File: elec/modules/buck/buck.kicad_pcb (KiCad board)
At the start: 2 copper layers, 35.6 x 40.6 mm, 18 parts, among them J1 Conn_01x08, J2 Conn_01x08, U2 TPS5430DDAG4, U3 TPS5430DDAG4

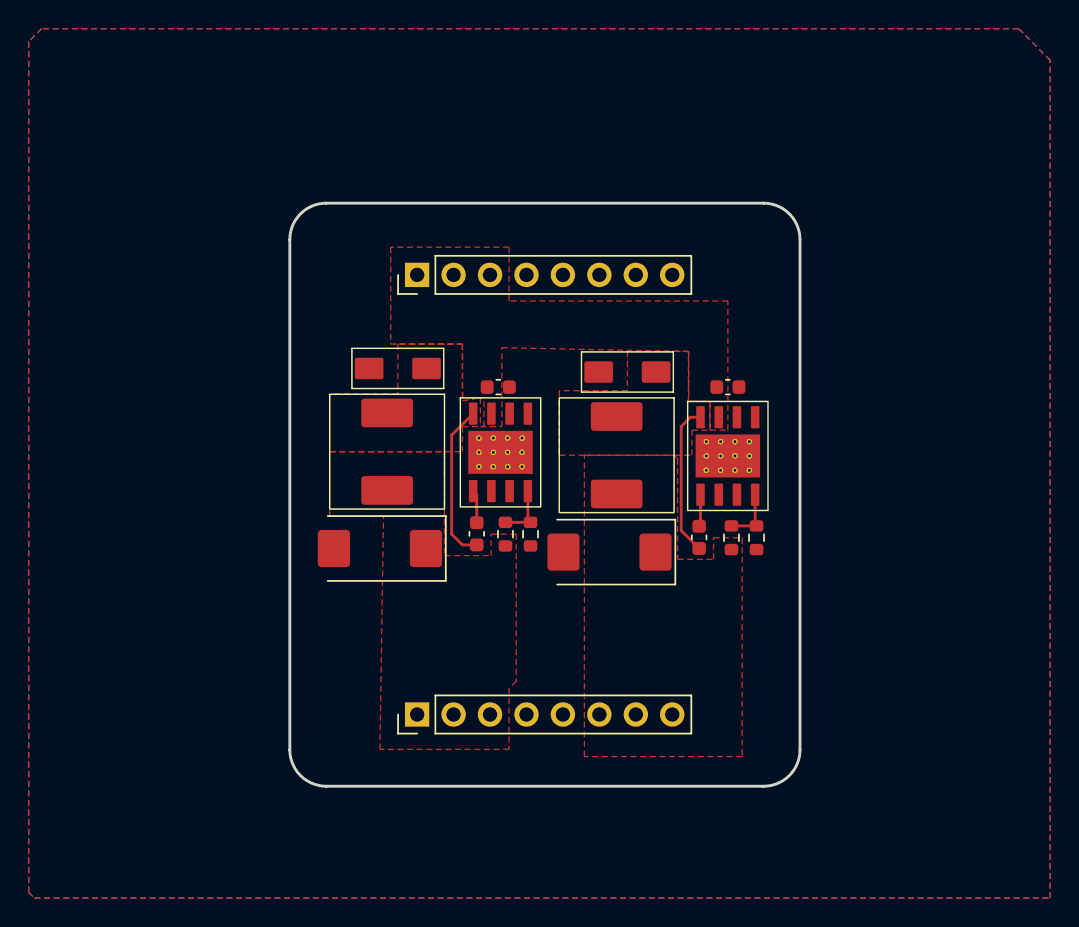
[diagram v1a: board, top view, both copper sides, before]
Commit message: Finished slaving avay buck done +PCBA
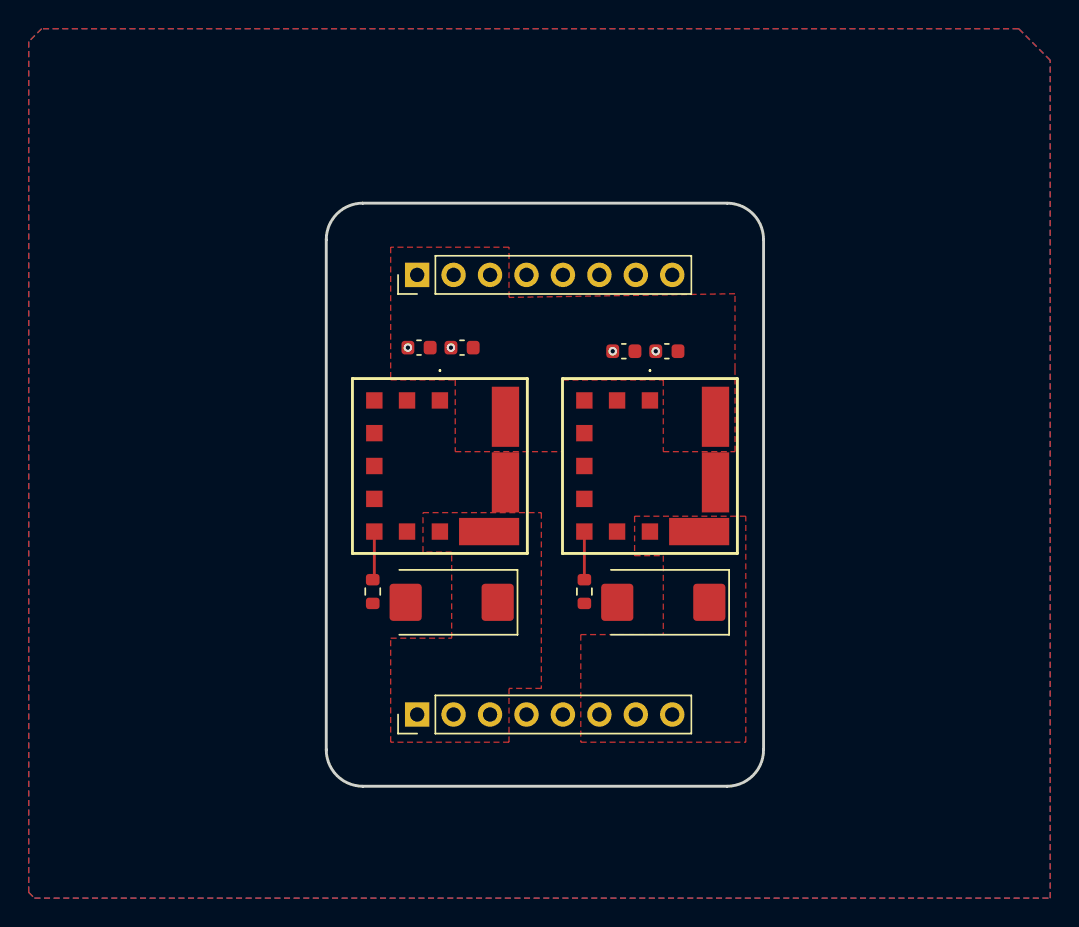
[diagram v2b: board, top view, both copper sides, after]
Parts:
- removed C8: 220u, Capacitor_Tantalum_SMD:CP_EIA-7343-15_Kemet-W_HandSolder
- removed D1, D2: SS54, Buckies:DIOM5025X220N
- removed L1, L2: 15uH, Buckies:0630 One Piece Inductor
- removed R10, R28: 10K, Resistor_SMD:R_0603_1608Metric
- removed R11: 5k9, Resistor_SMD:R_0603_1608Metric
- removed R37: 3K24, Resistor_SMD:R_0603_1608Metric
- removed U2, U3: TPS5430DDAG4, Buckies:TI_SO-PowerPAD-8
- added C4: 10u, Capacitor_SMD:C_0603_1608Metric, F.Cu at (144.8, 81.8)
- added PS1: OKL-T_6-W12P-C, Buck:OKLT6W12PC, F.Cu at (129.0, 89.8)
- added PS2: OKL-T_6-W12P-C, Buck:OKLT6W12PC, F.Cu at (143.6, 89.8)
- added R1: 1.33k, Resistor_SMD:R_0603_1608Metric, F.Cu at (124.3, 98.5)
- added R2: 2.18k, Resistor_SMD:R_0603_1608Metric, F.Cu at (139.0, 98.5)
- C2: value 10u -> 22u
- C3: value 10n -> 22u
- C6: value 10n -> 220u; footprint Capacitor_SMD:C_0603_1608Metric -> Capacitor_Tantalum_SMD:CP_EIA-7343-15_Kemet-W_HandSolder
- moved C1 21.7 mm to (127.5, 81.5), turned to 180 degrees
- moved C3 16.3 mm to (141.8, 81.8), turned to 180 degrees
- moved C5 6.25 mm to (129.8, 99.3)
- moved C6 5.17 mm to (144.5, 99.3), turned to 180 degrees
- moved C2 3.73 mm to (130.5, 81.5), turned to 180 degrees
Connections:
- C3 pad 1: Net-(U2-BOOT) -> +12V
- C3 pad 2: Net-(D1-K) -> GND
- C6 pad 1: Net-(U3-BOOT) -> +3V3
- C6 pad 2: Net-(D2-K) -> GND
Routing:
- net Net-(D1-K): track 11.1 -> 0.00 mm
- net Net-(D2-K): track 10.6 -> 0.00 mm
- net Net-(U2-VSENSE): track 4.00 -> 0.00 mm
- net Net-(U3-VSENSE): track 3.96 -> 0.00 mm
- net Net-(PS1-TRIM): track 0.00 -> 3.40 mm
- net Net-(PS2-TRIM): track 0.00 -> 3.36 mm
- net Net-(U2-BOOT): track 2.30 -> 0.00 mm
- net Net-(U3-BOOT): track 2.24 -> 0.00 mm
- net GND: vias 0 -> 4
- removed copper zone on F.Cu, net Net-(D1-K)
- removed copper zone on F.Cu, net Net-(D2-K)
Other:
- board size 35.6 x 40.6 mm -> 30.5 x 40.6 mm

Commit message: added v1 to bucks
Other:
- board text added: "design of 2-Chairs. 2025 JLC Order No. JLCJLCJLCJLC Version 1.0 (11/30/2025)"
- board text removed: "design of 2-Chairs. 2025 JLC Order No. JLCJLCJLCJLC"
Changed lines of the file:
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@@
 		(layer "Edge.Cuts")
 	)
-	(gr_text "design of 2-Chairs. 2025\nJLC Order No. JLCJLCJLCJLC"
+	(gr_text "design of 2-Chairs. 2025\nJLC Order No. JLCJLCJLCJLC\nVersion 1.0 (11/30/2025)"
 		(at 136.28 91.779999 0)
 		(layer "B.SilkS")

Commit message: added name cos why not
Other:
- board text added: "Design By Euston Tan"
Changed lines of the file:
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@@
+		)
+	)
+	(gr_text "Design By Euston Tan \n"
+		(at 136.28 110.529999 0)
+		(layer "B.SilkS")
+		(effects
+			(font
+				(size 1 1)
+				(thickness 0.2)
+				(bold yes)
+			)
+			(justify mirror)
 		)
 	)

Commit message: chore: buck production files
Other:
- board text added: "design of 2-Chairs. 2025 JLC Order No. JLCJLCJLCJLC rev. 1.0"
- board text removed: "design of 2-Chairs. 2025 JLC Order No. JLCJLCJLCJLC Version 1.0 (11/30/2025)"
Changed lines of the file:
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@@
 		(layer "Edge.Cuts")
 	)
-	(gr_text "design of 2-Chairs. 2025\nJLC Order No. JLCJLCJLCJLC\nVersion 1.0 (11/30/2025)"
+	(gr_text "design of 2-Chairs. 2025\nJLC Order No. JLCJLCJLCJLC\nrev. 1.0"
 		(at 136.28 91.779999 0)
 		(layer "B.SilkS")
@@
 	)
 	(gr_text "Design By Euston Tan \n"
-		(at 136.28 110.529999 0)
+		(at 136.28 109.979999 0)
 		(layer "B.SilkS")
 		(effects

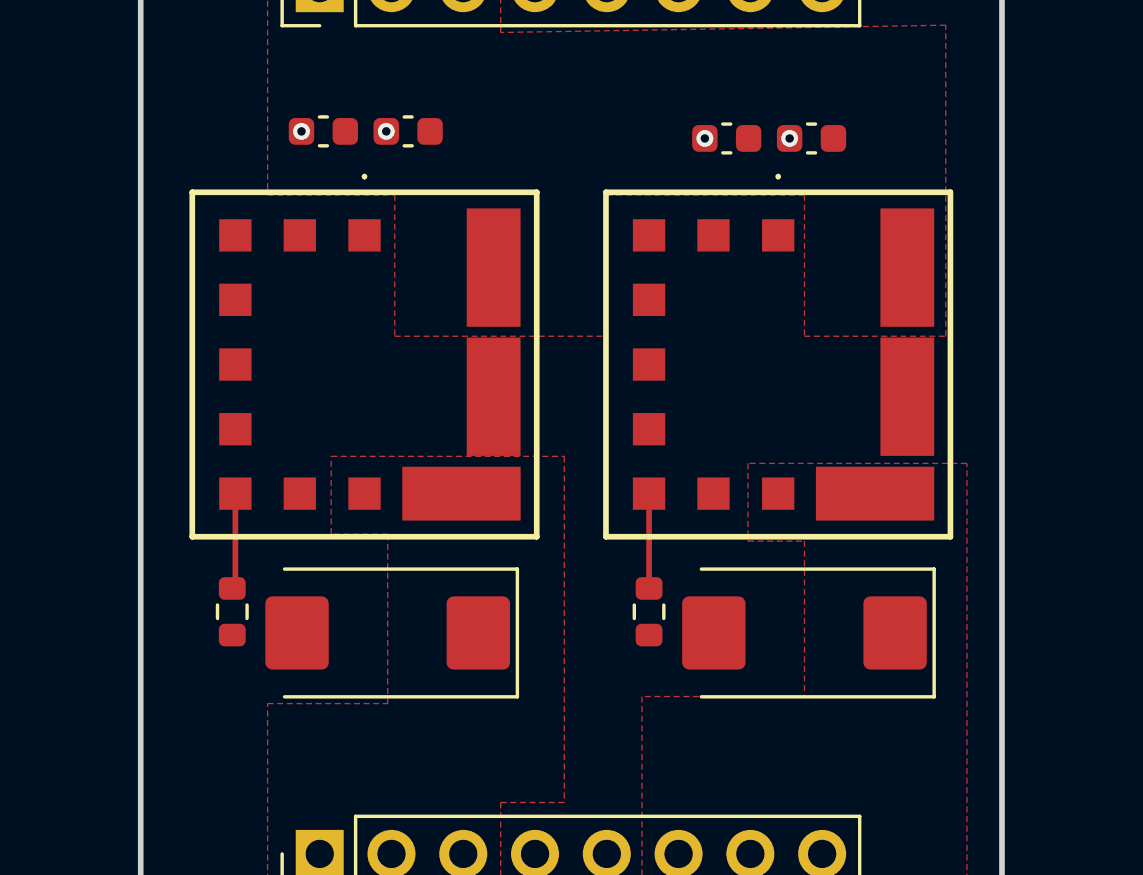
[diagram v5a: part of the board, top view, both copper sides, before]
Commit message: changed buck footprint
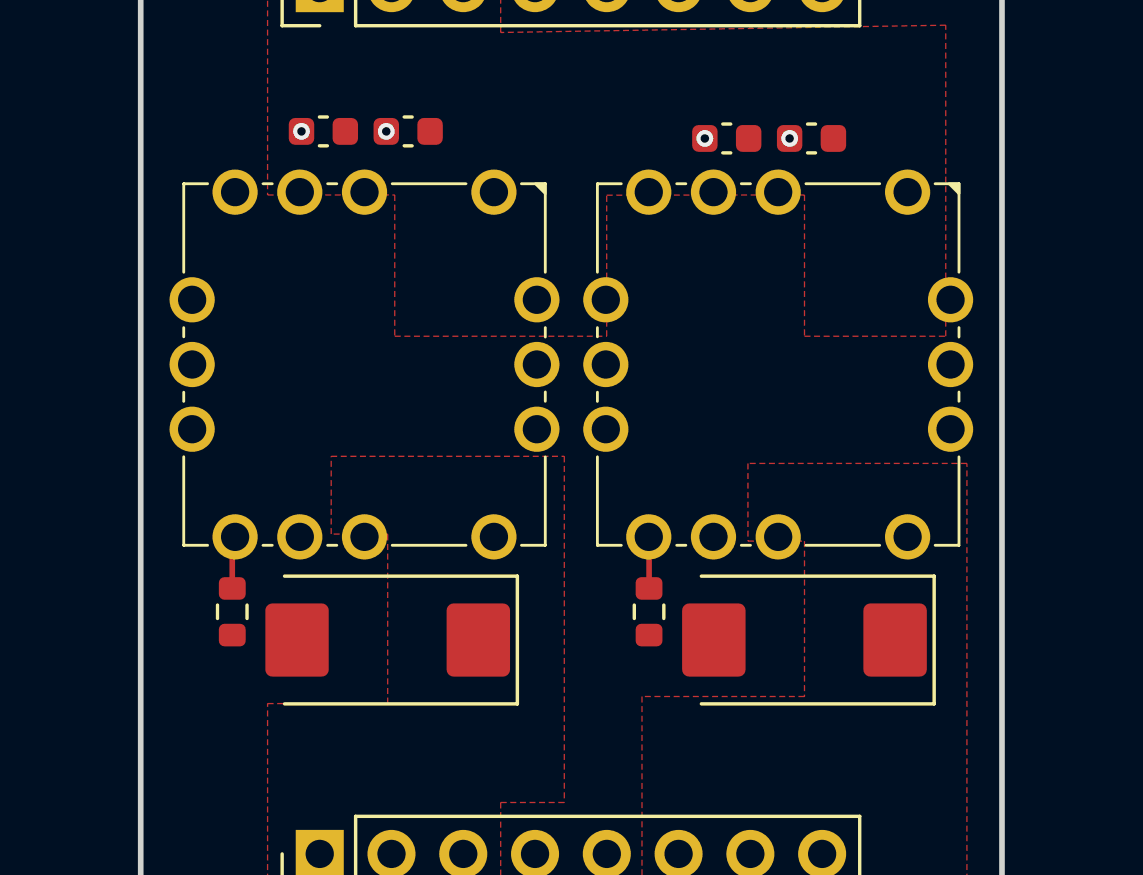
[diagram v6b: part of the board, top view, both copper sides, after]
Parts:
- PS1, PS2: footprint Buck:OKLT6W12PC -> Buck:MURATA_OKL-T-6-W12
- moved C5 0.25 mm to (129.8, 99.5)
- moved C6 0.25 mm to (144.5, 99.5)
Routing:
- net Net-(PS2-TRIM): track 3.36 -> 1.83 mm
- net Net-(PS1-TRIM): track 3.40 -> 2.02 mm
